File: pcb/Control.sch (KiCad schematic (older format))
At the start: 29 parts, among them SW1 Pulsador_2p, U1 ATMEGA328, U2 PCA9685, U3 FT231X, Y1 16MHz

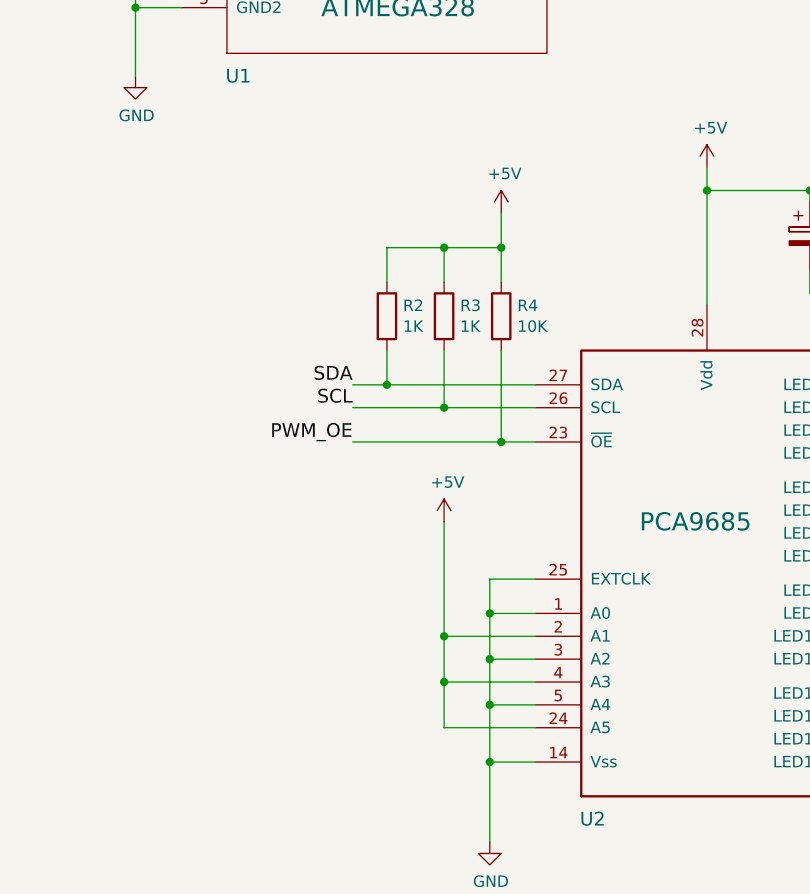
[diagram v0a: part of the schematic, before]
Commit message: modificar direccion I2C y pin /OE
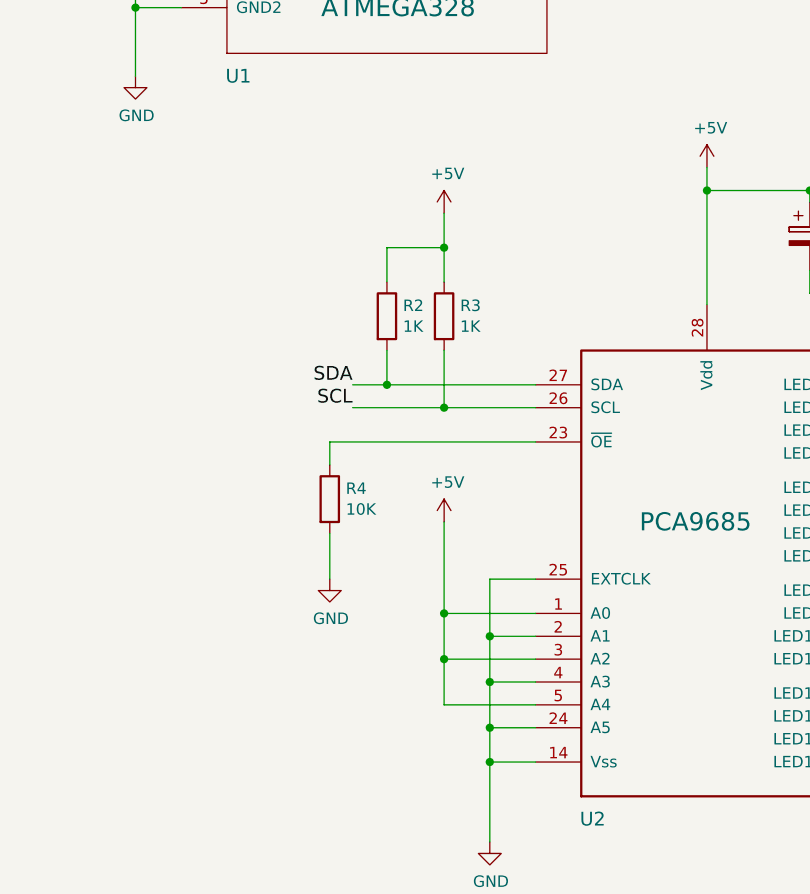
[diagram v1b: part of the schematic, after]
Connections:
- net +5V: now also U2.1 (A0), U2.3 (A2), U2.5 (A4); no longer R4.1, U2.2 (A1), U2.24 (A5), U2.4 (A3)
- net GND: now also R4.2, U2.2 (A1), U2.24 (A5), U2.4 (A3); no longer U2.1 (A0), U2.3 (A2), U2.5 (A4)
- net PWM_OE: no longer names the net of U2.23 (~OE)
- net PWM_OE: now also R4.1; no longer R4.2
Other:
- moved on the sheet: R4
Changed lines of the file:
@@
 	3200 5550 4000 5550
 Wire Wire Line
-	3200 5700 4000 5700
-Text Label 3200 5700 2    60   ~ 0
-PWM_OE
+	3100 5700 4000 5700
 Text Label 3200 5550 2    60   ~ 0
 SCL
@@
 L R R4
 U 1 1 576F3B45
-P 3850 5150
-F 0 "R4" H 3920 5196 50  0000 L CNN
-F 1 "10K" H 3920 5105 50  0000 L CNN
-F 2 "Resistors_SMD:R_0805" V 3780 5150 50  0001 C CNN
-F 3 "" H 3850 5150 50  0000 C CNN
-F 4 "vishay" H 1800 3700 60  0001 C CNN "Fabricante"
-F 5 "CRCW080510K0FKEA" H 1800 3700 60  0001 C CNN "Ref"
-F 6 "0.125W" H 1800 3700 60  0001 C CNN "Potencia"
-F 7 "1%" H 1800 3700 60  0001 C CNN "Tolerancia"
-F 8 "tme" H 1800 3700 60  0001 C CNN "Provedor"
-F 9 "CRCW080510K0FKEA" H 1800 3700 60  0001 C CNN "Ref_Proveedor"
-	1    3850 5150
+P 3100 5950
+F 0 "R4" H 3170 5996 50  0000 L CNN
+F 1 "10K" H 3170 5905 50  0000 L CNN
+F 2 "Resistors_SMD:R_0805" V 3030 5950 50  0001 C CNN
+F 3 "" H 3100 5950 50  0000 C CNN
+F 4 "vishay" H 1050 4500 60  0001 C CNN "Fabricante"
+F 5 "CRCW080510K0FKEA" H 1050 4500 60  0001 C CNN "Ref"
+F 6 "0.125W" H 1050 4500 60  0001 C CNN "Potencia"
+F 7 "1%" H 1050 4500 60  0001 C CNN "Tolerancia"
+F 8 "tme" H 1050 4500 60  0001 C CNN "Provedor"
+F 9 "CRCW080510K0FKEA" H 1050 4500 60  0001 C CNN "Ref_Proveedor"
+	1    3100 5950
 	1    0    0    -1
 $EndComp
-Wire Wire Line
-	3850 5300 3850 5700
-Connection ~ 3850 5700
 Wire Wire Line
 	3600 5550 3600 5300
@@
 Wire Wire Line
 	3350 5000 3350 4850
-Wire Wire Line
-	3350 4850 3850 4850
-Wire Wire Line
-	3850 4700 3850 5000
-Connection ~ 3850 4850
 $Comp
 L +5V #PWR013
 U 1 1 576F3E7D
-P 3850 4700
-F 0 "#PWR013" H 3850 4550 50  0001 C CNN
-F 1 "+5V" H 3865 4873 50  0000 C CNN
-F 2 "" H 3850 4700 50  0000 C CNN
-F 3 "" H 3850 4700 50  0000 C CNN
-	1    3850 4700
+P 3600 4700
+F 0 "#PWR013" H 3600 4550 50  0001 C CNN
+F 1 "+5V" H 3615 4873 50  0000 C CNN
+F 2 "" H 3600 4700 50  0000 C CNN
+F 3 "" H 3600 4700 50  0000 C CNN
+	1    3600 4700
 	1    0    0    -1
 $EndComp
 Wire Wire Line
-	3600 4850 3600 5000
+	3600 4700 3600 5000
 Connection ~ 3600 4850
 $Comp
@@
 $EndComp
 Wire Wire Line
-	3600 6050 3600 6950
-Wire Wire Line
-	3600 6950 4000 6950
-Wire Wire Line
-	4000 6750 3600 6750
-Connection ~ 3600 6750
-Wire Wire Line
-	3600 6550 4000 6550
-Connection ~ 3600 6550
-Wire Wire Line
 	4000 6300 3800 6300
 Connection ~ 3800 7100
 Wire Wire Line
-	3800 6850 4000 6850
-Connection ~ 3800 6850
-Wire Wire Line
-	4000 6650 3800 6650
-Connection ~ 3800 6650
-Wire Wire Line
-	3800 6450 4000 6450
-Connection ~ 3800 6450
+	3600 6850 4000 6850
+Wire Wire Line
+	3600 6650 4000 6650
+Wire Wire Line
+	3600 6450 4000 6450
 Text GLabel 4550 2450 2    60   Output ~ 0
 ENC1_A2
@@
 Text Notes 8800 6250 0    60   ~ 0
 Driver 1 \nStatus
+Wire Wire Line
+	3350 4850 3600 4850
+Wire Wire Line
+	3100 5700 3100 5800
+Wire Wire Line
+	3100 6100 3100 6300
+$Comp
+L GND #PWR021
+U 1 1 57B61664
+P 3100 6300
+F 0 "#PWR021" H 3100 6050 50  0001 C CNN
+F 1 "GND" H 3105 6127 50  0000 C CNN
+F 2 "" H 3100 6300 50  0000 C CNN
+F 3 "" H 3100 6300 50  0000 C CNN
+	1    3100 6300
+	1    0    0    -1
+$EndComp
+Connection ~ 3600 6450
+Connection ~ 3600 6650
+Wire Wire Line
+	3800 6750 4000 6750
+Connection ~ 3800 6750
+Wire Wire Line
+	4000 6550 3800 6550
+Connection ~ 3800 6550
+Wire Wire Line
+	3600 6850 3600 6050
+Wire Wire Line
+	4000 6950 3800 6950
+Connection ~ 3800 6950
 $EndSCHEMATC
